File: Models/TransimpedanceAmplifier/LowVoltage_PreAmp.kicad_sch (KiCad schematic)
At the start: 6 parts, among them U10 LM78L05, 5V, 5%, U8 TLV76133, 3.3V, 1%

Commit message: Save progress after a major refactoring
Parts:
- removed C10: 10 nF, symbol Device:C
- removed C9: 1 uF, symbol Device:C
- removed D10, D11: D_Schottky, symbol Device:D_Schottky
- removed U10: LM78L05, 5V, 5%, LP3_TEX, symbol LM78L:LM78L05ACZ_LFT1
- removed U8: TLV76133, 3.3V, 1%, DCY0004A-IPC_A, symbol TLV761:PTLV76118DCYR
- added C5: 10 nF, symbol Device:C
- added C6: 100 nF, symbol Device:C
- added D4, D5: D_Schottky, symbol Device:D_Schottky
- added U7: LM78L05, 5V, 5%, LP3_TEX, symbol LM78L:LM78L05ACZ_LFT1
- added U9: LM79L05, -5V, 5%, LP3_TEX, symbol LM79L:LM79L05ACZ_LFT1
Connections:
- net 5V: now also C5.1, D4.1 (K), U7.1 (OUTPUT)
- net GND: now also C5.2, C6.1, D4.2 (A), D5.1 (K), U7.2 (GND), U9.1 (GND)
- new net -15V: U9.2 (-VIN)
- new net -5V: C6.2, D5.2 (A), U9.3 (-VOUT)
- new net 15V: U7.3 (INPUT)
- no-connect marks 1 -> 0
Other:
- note removed: "Dropout voltage: 0.9 V (typical), 1.6 V (max) Variation with load: 0.9 V (1.0 A) 0.7 V (0.8 A) 0.2 V (0.1 A) Dropout voltage exceeds expected value when Vout + 1.5 V < 4.0 V"

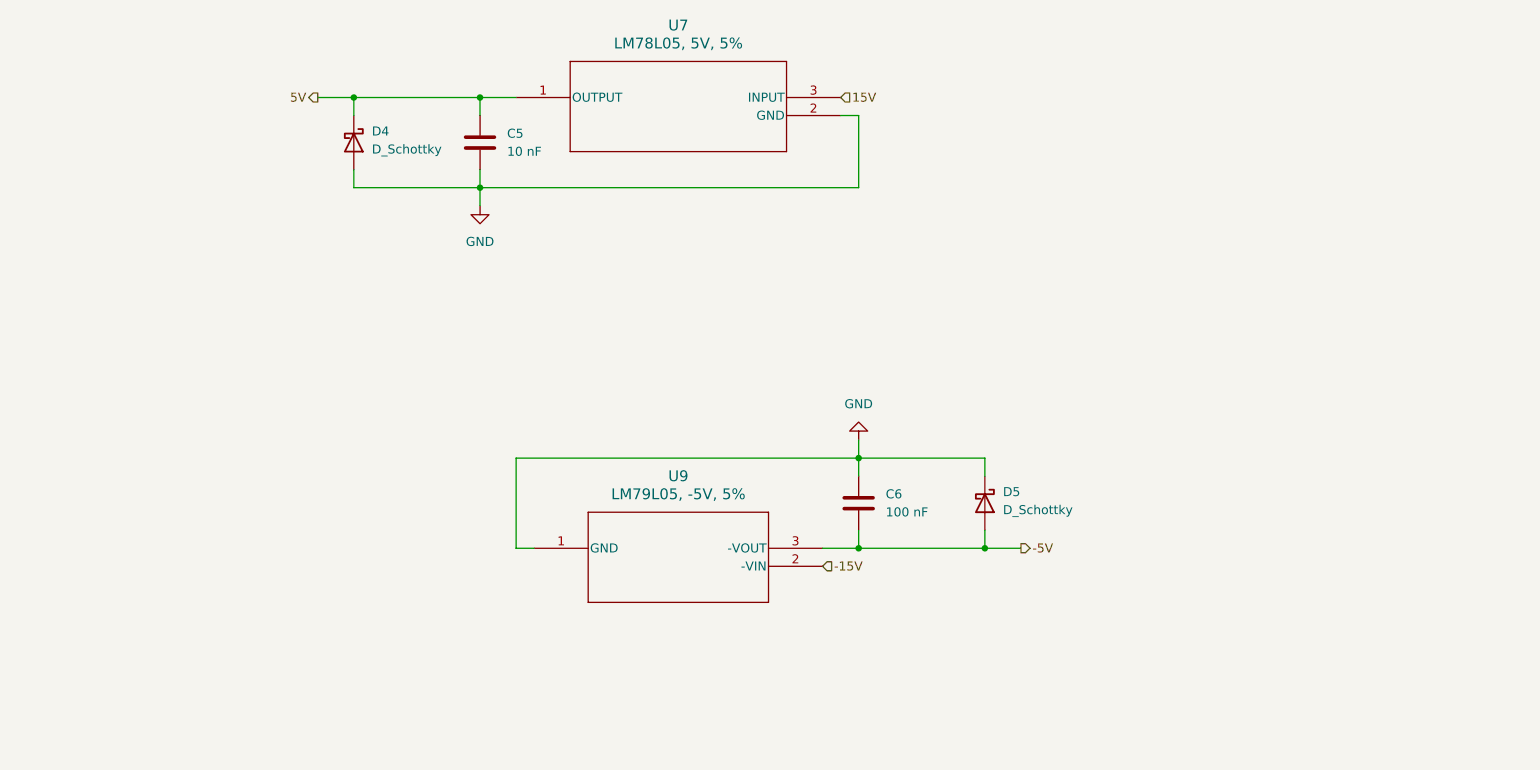
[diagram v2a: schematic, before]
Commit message: Added purchase links for all current capacitors, with dimensional tolerances matching the footprint
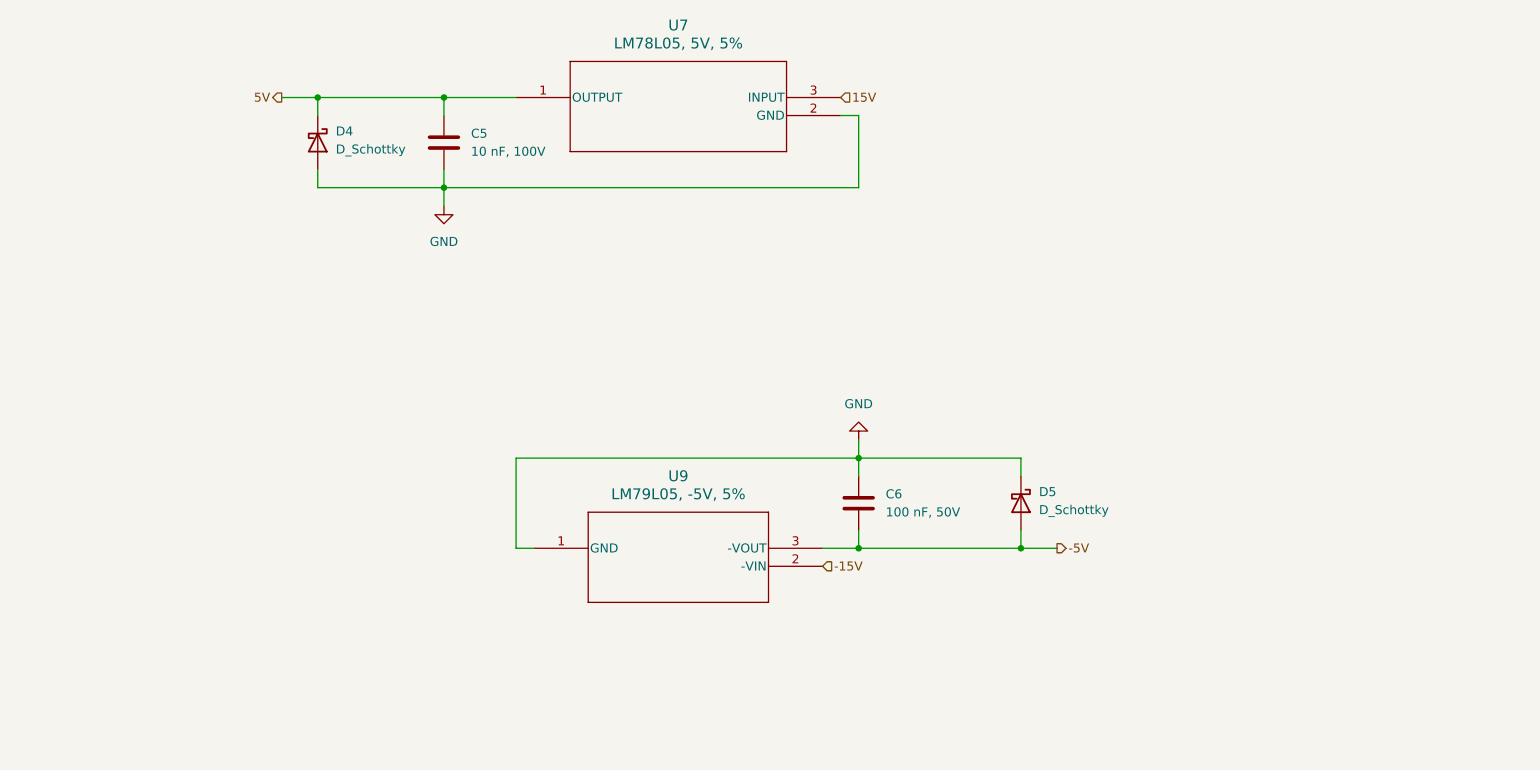
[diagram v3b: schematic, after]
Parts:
- C5: value 10 nF -> 10 nF, 100V; Purchase Link (none) -> https://www.digikey.com/en/products/detail/murata-electroni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
- C6: value 100 nF -> 100 nF, 50V; Purchase Link (none) -> https://www.digikey.com/en/products/detail/murata-electroni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
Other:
- moved on the sheet: C5, D4, D5

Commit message: All suppliers are out of stock of LM7915L in the simple TO-92-3 package. Resolve this by first tabulating the maximum possible current on each regulator.
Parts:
- U7, U9: Purchase Link (none) -> https://www.digikey.com/en/products/detail/texas-instrument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
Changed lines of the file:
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@@
+			)
+		)
+		(property "Purchase Link" "https://www.digikey.com/en/products/detail/texas-instruments/LM79L05ACZ-NOPB/1871963"
+			(at 121.92 119.38 0)
+			(effects
+				(font
+					(size 1.27 1.27)
+				)
+				(hide yes)
 			)
 		)
@@
 			)
 		)
-		(property "Purchase Link" ""
+		(property "Purchase Link" "https://www.digikey.com/en/products/detail/texas-instruments/LM78L05ACZ-NOPB/6333"
 			(at 119.38 55.88 0)
 			(effects

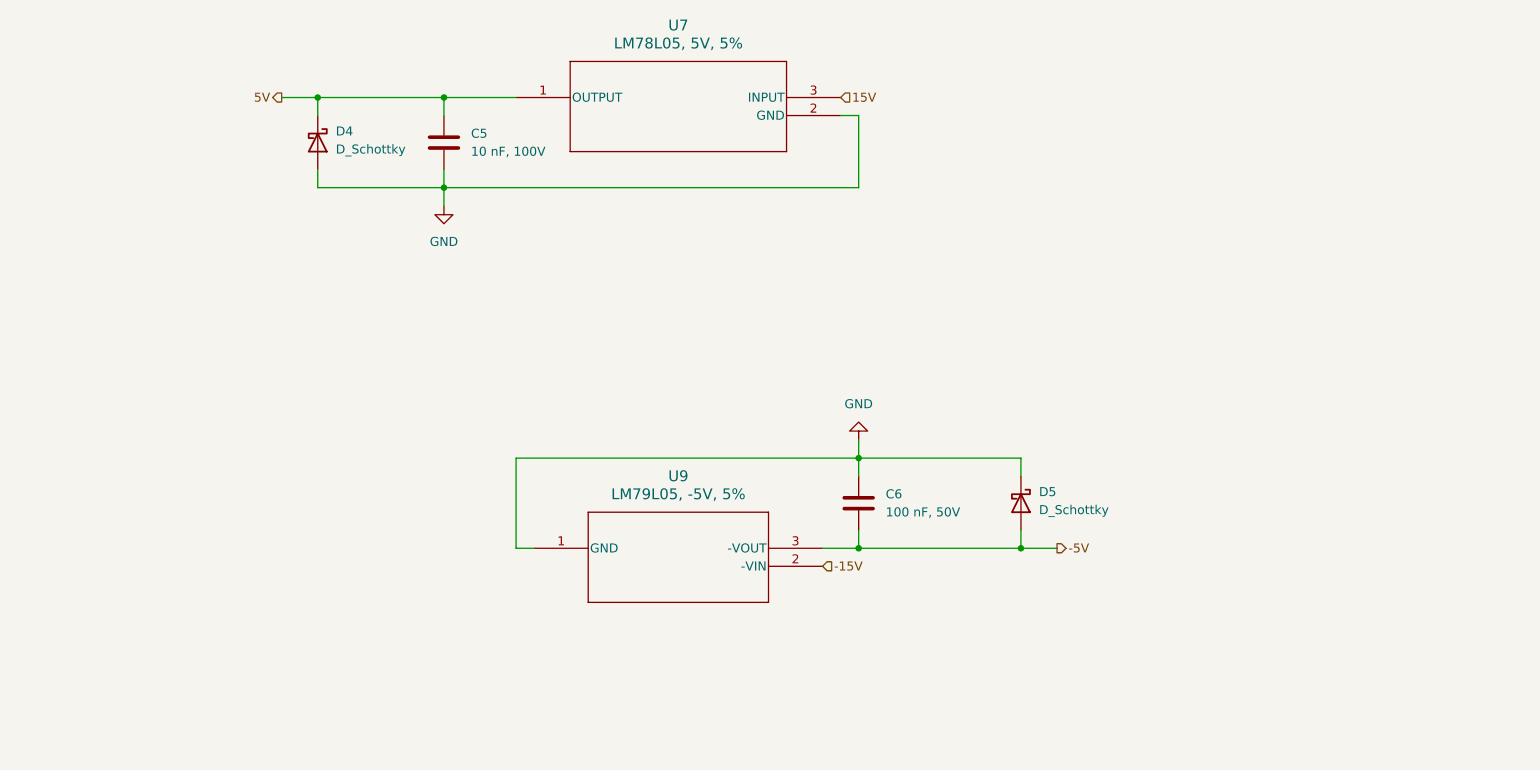
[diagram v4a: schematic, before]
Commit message: Removed all protection diodes for now
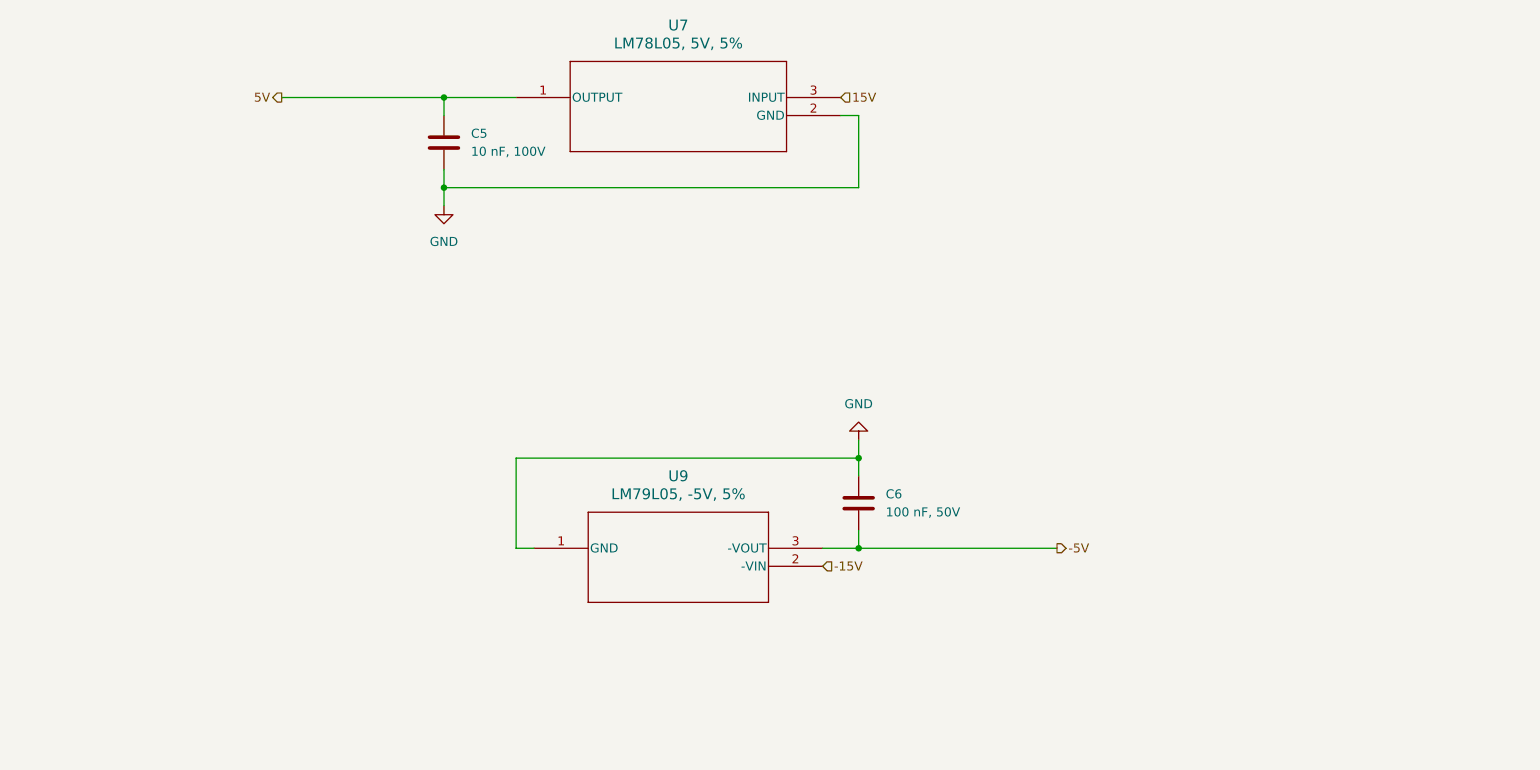
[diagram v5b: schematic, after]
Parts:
- removed D4, D5: D_Schottky, symbol Device:D_Schottky
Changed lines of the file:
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@@
 	(paper "A4")
-	(junction
-		(at 190.5 119.38)
-		(diameter 0)
-		(color 0 0 0 0)
-	)
 	(junction
 		(at 167.64 106.68)
@@
 	)
 	(junction
-		(at 91.44 55.88)
-		(diameter 0)
-		(color 0 0 0 0)
-	)
-	(junction
 		(at 109.22 68.58)
 		(diameter 0)
@@
 	(wire
 		(pts
-			(xy 167.64 119.38) (xy 190.5 119.38)
-		)
-		(stroke
-			(width 0)
-			(type default)
-		)
-	)
-	(wire
-		(pts
-			(xy 190.5 119.38) (xy 195.58 119.38)
+			(xy 167.64 119.38) (xy 195.58 119.38)
 		)
 		(stroke
@@
 	(wire
 		(pts
-			(xy 109.22 55.88) (xy 91.44 55.88)
-		)
-		(stroke
-			(width 0)
-			(type default)
-		)
-	)
-	(wire
-		(pts
-			(xy 86.36 55.88) (xy 91.44 55.88)
-		)
-		(stroke
-			(width 0)
-			(type default)
-		)
-	)
-	(wire
-		(pts
-			(xy 167.64 106.68) (xy 190.5 106.68)
-		)
-		(stroke
-			(width 0)
-			(type default)
-		)
-	)
-	(wire
-		(pts
-			(xy 91.44 66.04) (xy 91.44 68.58)
+			(xy 86.36 55.88) (xy 109.22 55.88)
 		)
 		(stroke
@@
 	(wire
 		(pts
-			(xy 91.44 68.58) (xy 109.22 68.58)
-		)
-		(stroke
-			(width 0)
-			(type default)
-		)
-	)
-	(wire
-		(pts
 			(xy 167.64 109.22) (xy 167.64 106.68)
 		)
@@
 	(wire
 		(pts
-			(xy 190.5 106.68) (xy 190.5 109.22)
-		)
-		(stroke
-			(width 0)
-			(type default)
-		)
-	)
-	(wire
-		(pts
 			(xy 167.64 116.84) (xy 167.64 119.38)
 		)
@@
 	(wire
 		(pts
-			(xy 91.44 55.88) (xy 91.44 58.42)
-		)
-		(stroke
-			(width 0)
-			(type default)
-		)
-	)
-	(wire
-		(pts
 			(xy 167.64 104.14) (xy 167.64 106.68)
-		)
-		(stroke
-			(width 0)
-			(type default)
-		)
-	)
-	(wire
-		(pts
-			(xy 190.5 116.84) (xy 190.5 119.38)
 		)
 		(stroke
@@
 					(unit 1)
 				)
-			)
-		)
-	)
-	(symbol
-		(lib_id "Device:D_Schottky")
-		(at 190.5 113.03 270)
-		(unit 1)
-		(exclude_from_sim no)
-		(in_bom yes)
-		(on_board yes)
-		(dnp no)
-		(fields_autoplaced yes)
-		(property "Reference" "D5"
-			(at 193.04 111.4424 90)
-			(effects
-				(font
-					(size 1.27 1.27)
-				)
-				(justify left)
-			)
-		)
-		(property "Value" "D_Schottky"
-			(at 193.04 113.9824 90)
-			(effects
-				(font
-					(size 1.27 1.27)
-				)
-				(justify left)
-			)
-		)
-		(property "Footprint" ""
-			(at 190.5 113.03 0)
-			(effects
-				(font
-					(size 1.27 1.27)
-				)
-				(hide yes)
-			)
-		)
-		(property "Datasheet" "~"
-			(at 190.5 113.03 0)
-			(effects
-				(font
-					(size 1.27 1.27)
-				)
-				(hide yes)
-			)
-		)
-		(property "Description" "Schottky diode"
-			(at 190.5 113.03 0)
-			(effects
-				(font
-					(size 1.27 1.27)
-				)
-				(hide yes)
-			)
-		)
-		(pin "2"
-		)
-		(pin "1"
-		)
-		(instances
-			(project ""
-				(path "/ec9f2ae3-e40d-40eb-9760-2b611ee8efd1/d0ece2d4-5b22-4822-ad0c-e2361683ec3d/ddbdd109-856f-45b9-b116-121e4fcc3b3f"
-					(reference "D5")
-					(unit 1)
-				)
-			)
-		)
-	)
-	(symbol
-		(lib_id "Device:D_Schottky")
-		(at 91.44 62.23 270)
-		(unit 1)
-		(exclude_from_sim no)
-		(in_bom yes)
-		(on_board yes)
-		(dnp no)
-		(fields_autoplaced yes)
-		(property "Reference" "D4"
-			(at 93.98 60.6424 90)
-			(effects
-				(font
-					(size 1.27 1.27)
-				)
-				(justify left)
-			)
-		)
-		(property "Value" "D_Schottky"
-			(at 93.98 63.1824 90)
-			(effects
-				(font
-					(size 1.27 1.27)
-				)
-				(justify left)
-			)
-		)
-		(property "Footprint" ""
-			(at 91.44 62.23 0)
-			(effects
-				(font
-					(size 1.27 1.27)
-				)
-				(hide yes)
-			)
-		)
-		(property "Datasheet" "~"
-			(at 91.44 62.23 0)
-			(effects
-				(font
-					(size 1.27 1.27)
-				)
-				(hide yes)
-			)
-		)
-		(property "Description" "Schottky diode"
-			(at 91.44 62.23 0)
-			(effects
-				(font
-					(size 1.27 1.27)
-				)
-				(hide yes)
-			)
-		)
-		(pin "1"
-		)
-		(pin "2"
-		)
-		(instances
-			(project ""
-				(path "/ec9f2ae3-e40d-40eb-9760-2b611ee8efd1/d0ece2d4-5b22-4822-ad0c-e2361683ec3d/ddbdd109-856f-45b9-b116-121e4fcc3b3f"
-					(reference "D4")
-					(unit 1)
-				)

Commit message: Deleted all schematics for voltage regulators
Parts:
- removed C5: 10 nF, 100V, symbol Device:C
- removed C6: 100 nF, 50V, symbol Device:C
- removed U7: LM78L05, 5V, 5%, LP3_TEX, symbol LM78L:LM78L05ACZ_LFT1
- removed U9: LM79L05, -5V, 5%, LP3_TEX, symbol LM79L:LM79L05ACZ_LFT1

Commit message: Finished rewriting the schematic, just need purchase links for the new regulators
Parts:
- added C5: 1 uF, 50V, symbol Device:C
- added U7: LM7805, 5V, 5%, NDE3_TEX, symbol LM78:LM7805CT_NOPB
- added U9: LM7905, -5V, 5%, T03B_TEX, symbol LM79:LM7905CT
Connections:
- new net -15V: U9.2 (IN)
- new net -5V: C5.1, U9.3 (OUT)
- new net 15V: U7.1 (INPUT)
- new net 5V: U7.3 (OUTPUT)
- new net GND: C5.2, U7.2 (GND), U9.1 (GND)

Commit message: Overhauled the purchase links for regulators and trimpots
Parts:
- U7, U9: Purchase Link (none) -> https://www.digikey.com/en/products/detail/texas-instrument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
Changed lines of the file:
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@@
+			)
+		)
+		(property "Purchase Link" "https://www.digikey.com/en/products/detail/texas-instruments/LM7905CT-NOPB/6349"
+			(at 175.26 81.28 0)
+			(effects
+				(font
+					(size 1.27 1.27)
+				)
+				(hide yes)
 			)
 		)
@@
 			(at 54.61 81.28 0)
 			(effects
+				(font
+					(size 1.27 1.27)
+				)
+				(hide yes)
+			)
+		)
+		(property "Purchase Link" "https://www.digikey.com/en/products/detail/texas-instruments/LM7805CT-NOPB/3901929"
+			(at 54.61 81.28 0)
+			(effects
